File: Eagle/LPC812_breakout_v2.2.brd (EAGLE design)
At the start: 27.9 x 15.2 mm, 13 parts

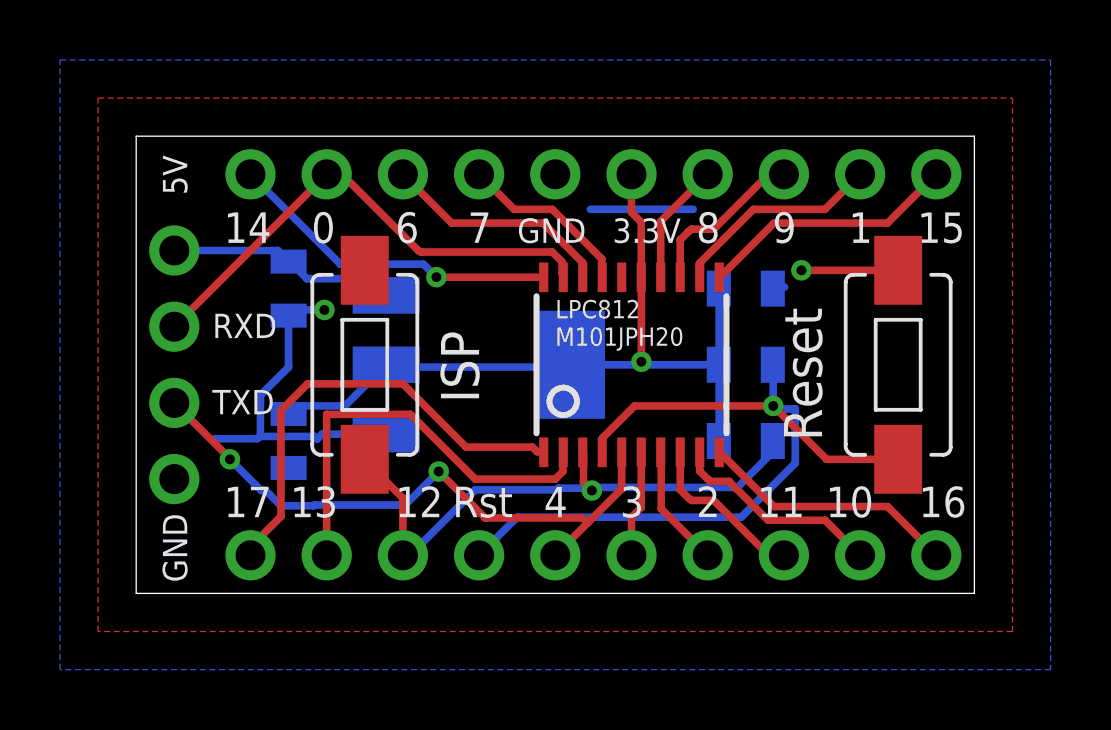
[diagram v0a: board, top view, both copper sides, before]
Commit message: Revision 2.2 -  Broke out 5V pin
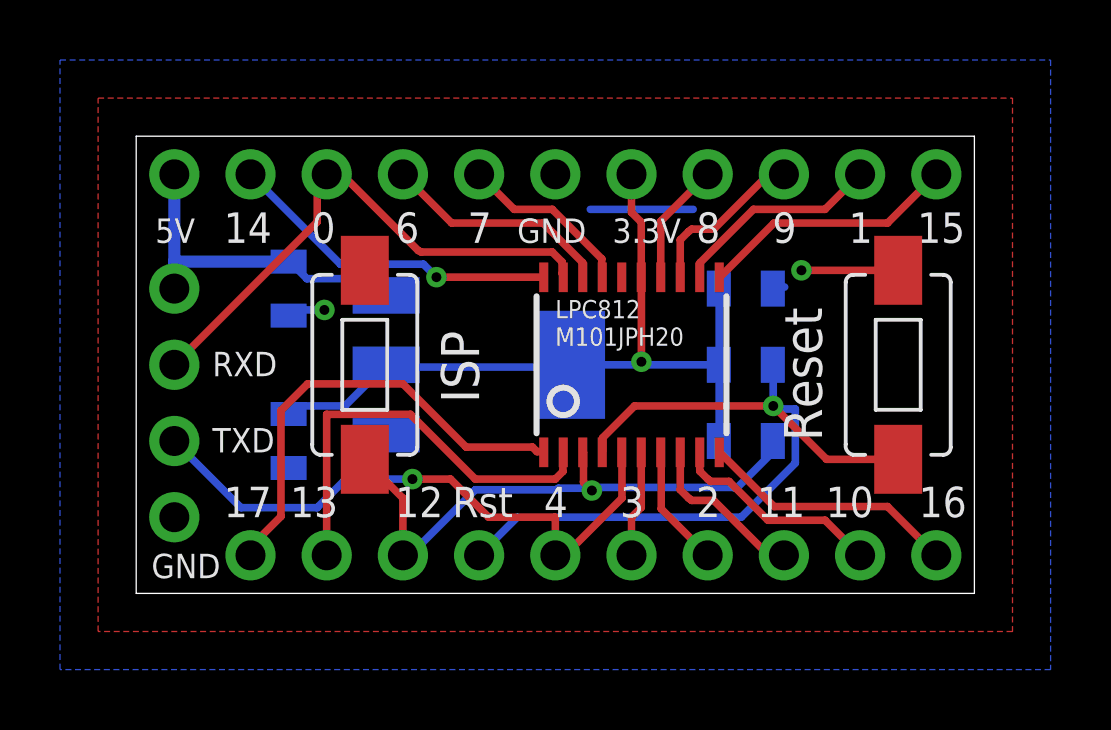
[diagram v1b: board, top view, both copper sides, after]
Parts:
- added JP4: (no value), microbuilder:1X01_ROUND
- moved JP3 1.27 mm to (1.27, 6.35)
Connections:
- net 5V: now also JP4.1
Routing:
- net GND: track 18.7 -> 8.47 mm
- net 5V: track 7.68 -> 11.4 mm
- net P19: track 16.8 -> 18.2 mm
- net P5: track 20.7 -> 20.4 mm, vias 2 -> 1
